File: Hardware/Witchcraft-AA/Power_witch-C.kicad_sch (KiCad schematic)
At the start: 11 parts, among them J3 Conn_01x05_Socket, U1 Z1 extreme, U2 LM26420-Q1xx-xxxx, U3 K3LKCKC0BM, U4 K3LKCKC0BM

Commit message: ECAD: replaced the Z1 Extreme with the 7840U chip, as the AI-engine will be more useful for makers and non-gamers. MCAD: continued converting the outer shell towards a Assembly4-architecture, adding more items. Started a big change in design wherein I'm splitting the shell-design into a modular one, to accomodate removable controllers. Made some minor tweaks to the cooling-assembly, to accomodate the new, split shell-design. Updated the Readme to describe the project.
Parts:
- removed J3: Conn_01x05_Socket, Connector_PinHeader_1.27mm:PinHeader_1x05_P1.27mm_Vertical_SMD_Pin1Left, symbol Connector:Conn_01x05_Socket
- added J2: ~, LRJ:Samsung_Hirose_xxx-xxx_2x3_P0.35mm_Vertical, symbol LRJ-parts:Samsung_power-con
- U1: value Z1 extreme -> AMD Ryzen 7840U; symbol LRJ-parts:AMD_Z1_extreme -> LRJ-parts:AMD_Ryzen_7840U_FP8; Details https://en.wikichip.org/wiki/amd/packages/socket_am5#Packag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 -> https://en.wikichip.org/wiki/amd/packages/fp6; Operating temperature (none) -> 0 C ~ 45 C
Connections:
- net +3.88V: now also J2.1 (VCC), J2.11 (VCC), J2.12 (VCC)
- net GND: now also U1.A190 (Vss), U1.A210 (Vss), U1.A230 (Vss), U1.A302 (Vss), U1.D14 (Vss), U1.E32 (Vss), J2.10 (GND), J2.2 (GND), J2.9 (GND); no longer U1.A14 (Vss), U1.A19 (Vss), U1.A21 (Vss), U1.A23 (Vss), U1.A3 (Vss), U1.C32 (Vss)

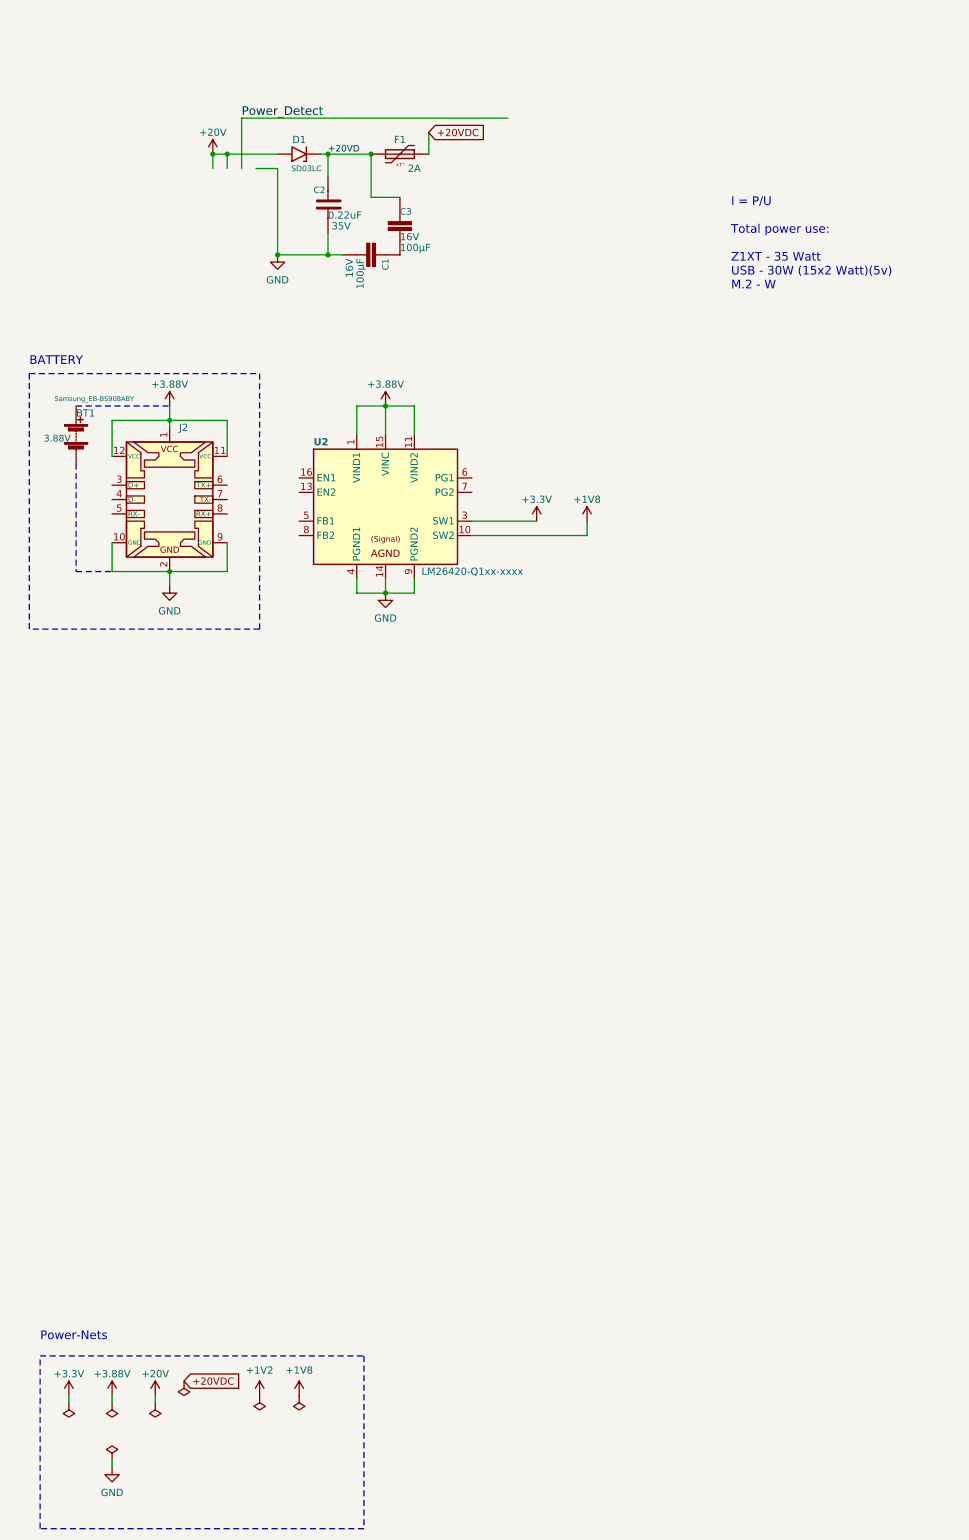
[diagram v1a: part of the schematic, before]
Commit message: MCAD: Added Oculink connector. ECAD: Added Oculink connector.
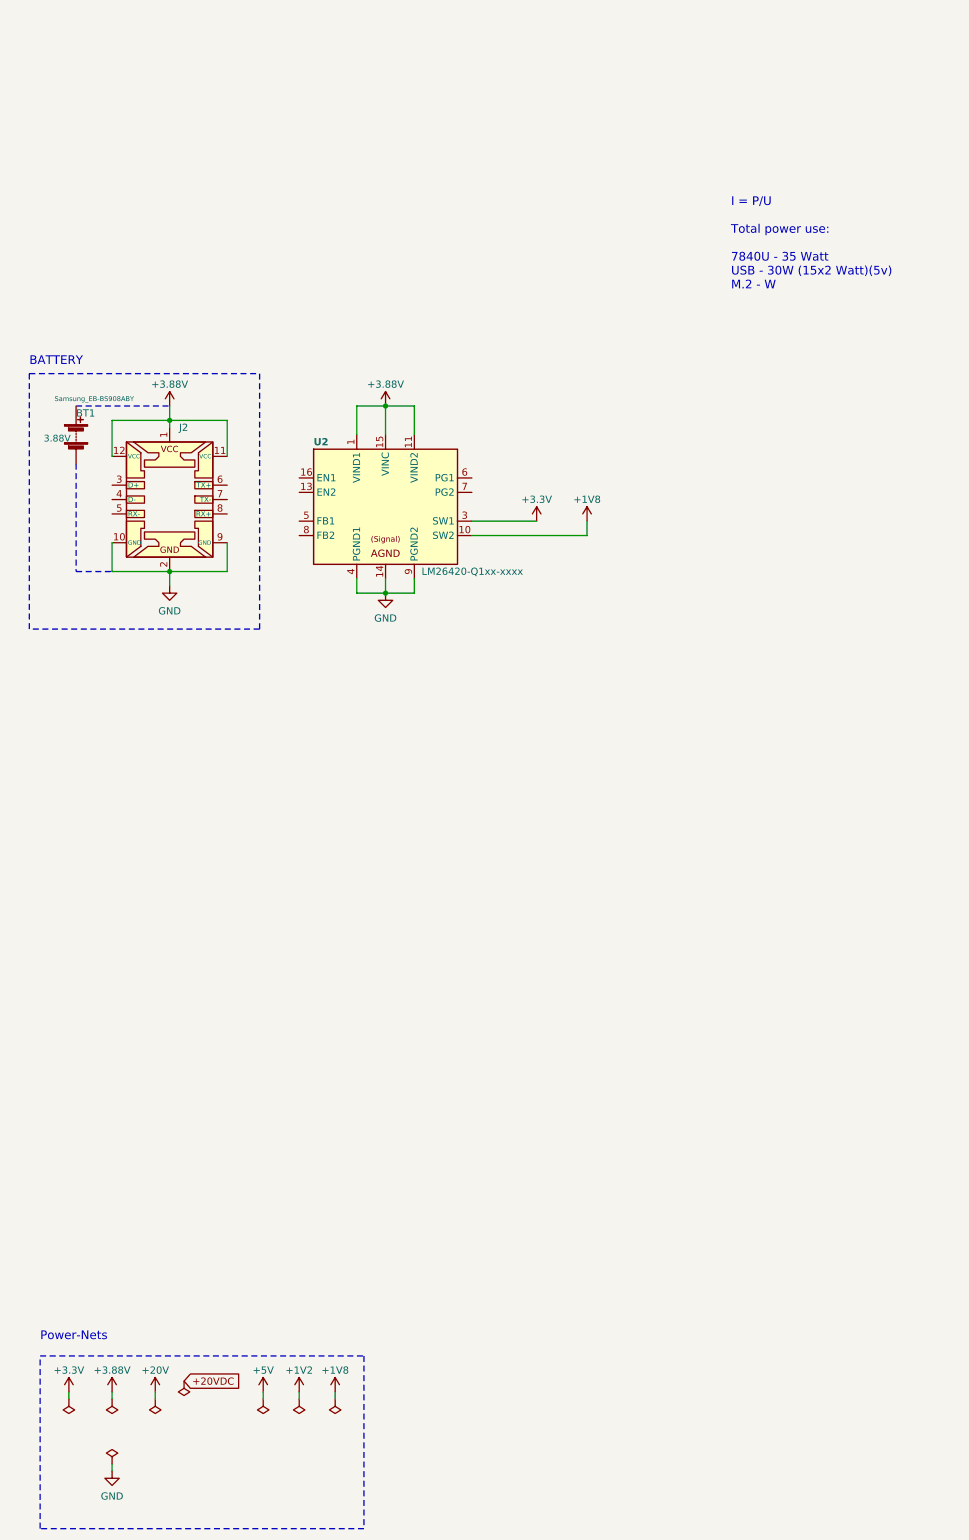
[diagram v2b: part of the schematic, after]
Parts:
- removed C1, C3: C_CC1210MKX5R7BB107, Capacitor_SMD:C_1210_3225Metric, symbol LRJ-parts:C_EMK325ABJ107MM
- removed C2: C_CGA2B1X7R1V224K, Capacitor_SMD:C_0402_1005Metric, symbol LRJ-parts:C_CGA2B1X7R1V224K
- removed D1: SD03LC, Diode_SMD:D_SOD-323, symbol LRJ-parts:D_SD03LC
- removed F1: PPTC_SMD2920B200, LRJ:Fuse_Yageo_SMD2920B200TF_L7.3mm_W5.1mm, symbol LRJ-parts:PPTC_SMD2920B200
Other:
- note added: "I = P/U Total power use: 7840U - 35 Watt USB - 30W (15x2 Watt)(5v) M.2 - W"
- note removed: "I = P/U Total power use: Z1XT - 35 Watt USB - 30W (15x2 Watt)(5v) M.2 - W"
- title: (none) -> WITCHCRAFT HANDHELD
